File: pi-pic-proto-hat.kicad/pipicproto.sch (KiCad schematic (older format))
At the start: 39 parts, among them J1 RUN/~PGM~, J10 Conn_01x13_Male, J11 Conn_5P_2, J12 Conn_01x01_Male, J13 Conn_01x05_Male, J14 Conn_01x02_Male, J2 Conn_SW1, J22 Conn_01x13_Male, J3 Conn_5P, J4 Conn_3V3P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

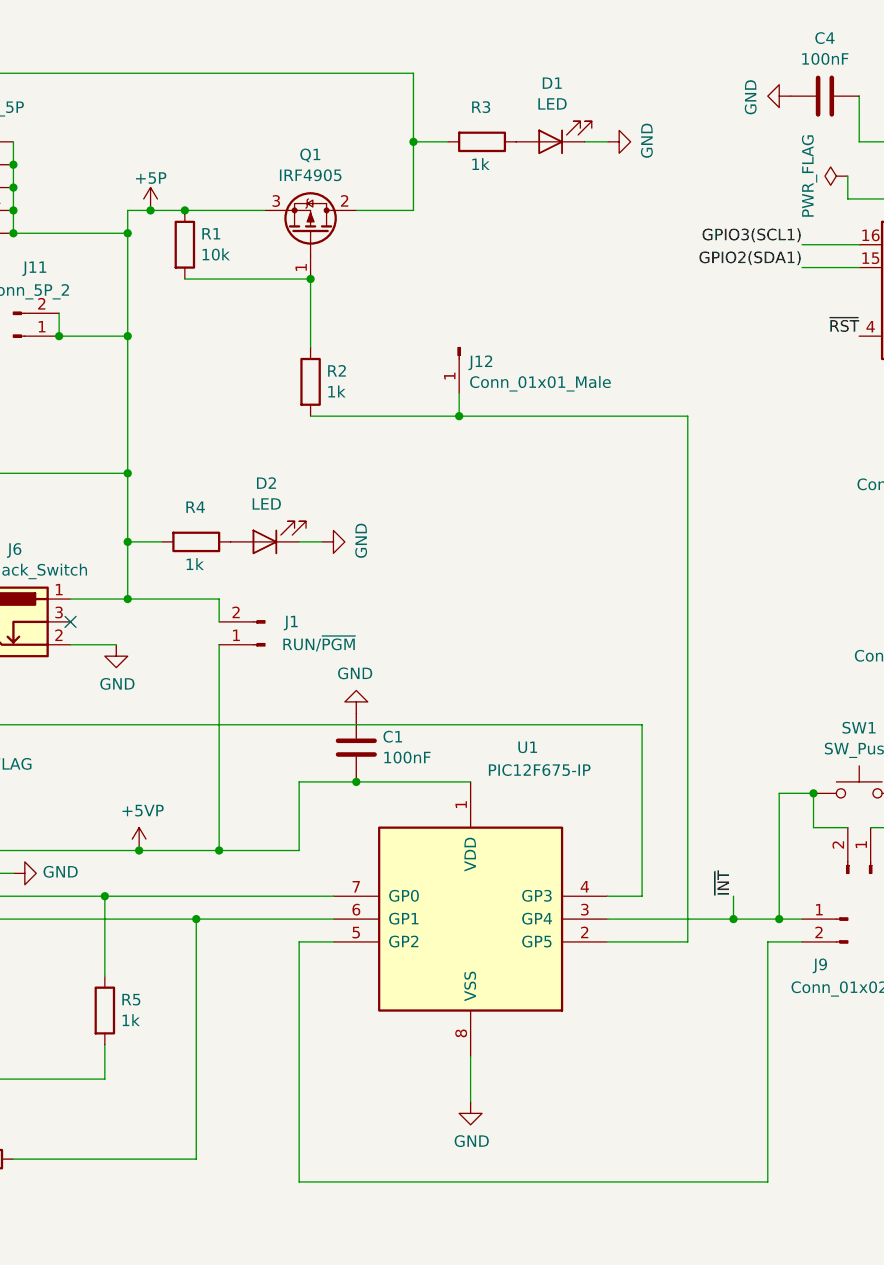
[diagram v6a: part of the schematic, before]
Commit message: non-functional changes to layout
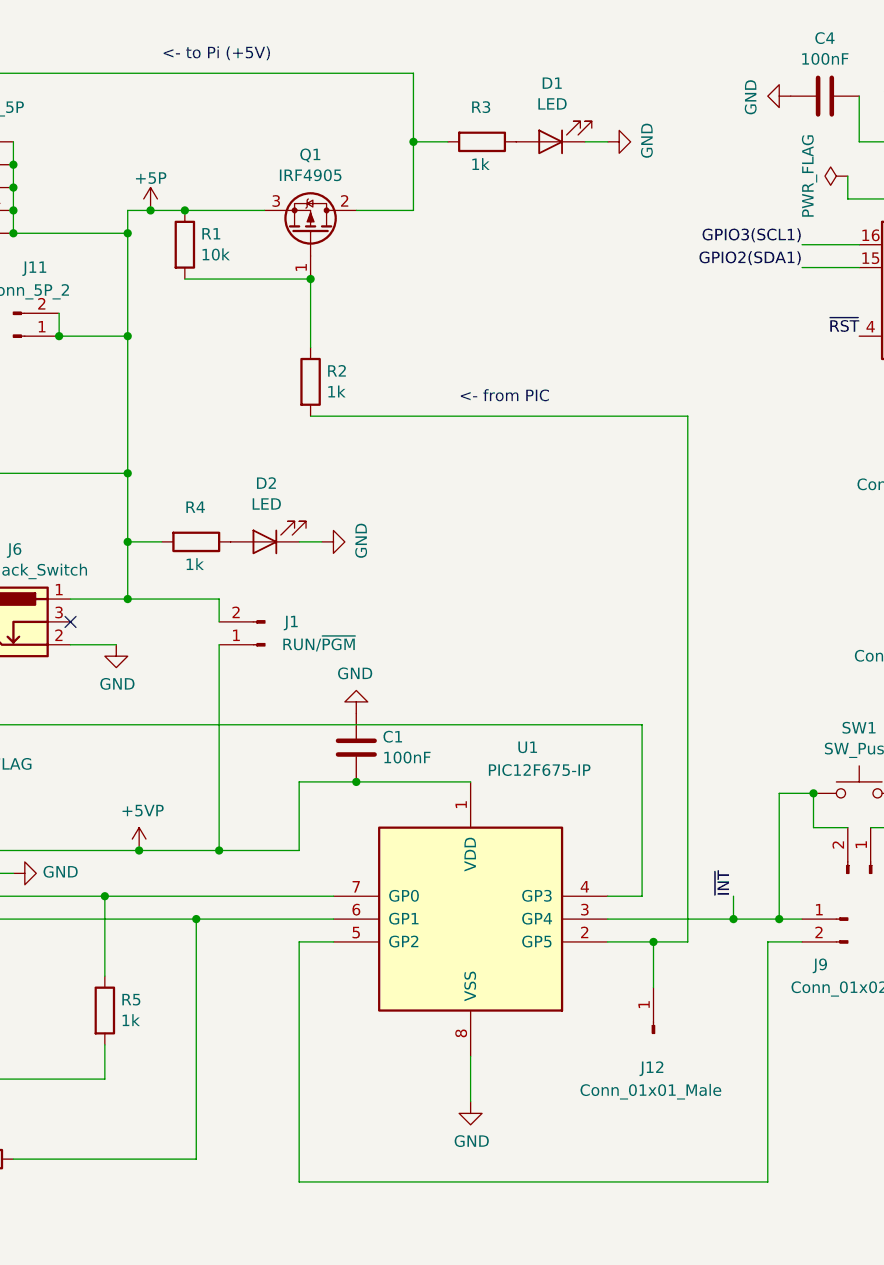
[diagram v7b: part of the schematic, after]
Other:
- note added: "<- from PIC"
- note added: "<- to Pi (+5V)"
- moved on the sheet: J12
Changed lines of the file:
@@
 	1700 4950 1700 5850
 Wire Wire Line
-	8600 4700 8950 4700
-Wire Wire Line
-	8950 4700 8950 2400
-Wire Wire Line
-	8950 2400 7950 2400
+	8600 4700 8800 4700
 Text Label 5850 5300 2    50   ~ 0
 GPIO16
@@
 L Connector:Conn_01x01_Male J12
 U 1 1 5F23F4B8
-P 7950 2100
-F 0 "J12" V 8012 2144 50  0000 L CNN
-F 1 "Conn_01x01_Male" V 8103 2144 50  0000 L CNN
-F 2 "Connector_PinHeader_2.54mm:PinHeader_1x01_P2.54mm_Vertical" H 7950 2100 50  0001 C CNN
-F 3 "~" H 7950 2100 50  0001 C CNN
-	1    7950 2100
-	0    1    1    0
-$EndComp
-Wire Wire Line
-	7950 2400 7950 2300
-Connection ~ 7950 2400
-Wire Wire Line
-	7950 2400 7300 2400
+P 8800 5100
+F 0 "J12" V 8650 5050 50  0000 L CNN
+F 1 "Conn_01x01_Male" V 8550 4800 50  0000 L CNN
+F 2 "Connector_PinHeader_2.54mm:PinHeader_1x01_P2.54mm_Vertical" H 8800 5100 50  0001 C CNN
+F 3 "~" H 8800 5100 50  0001 C CNN
+	1    8800 5100
+	0    -1   -1   0
+$EndComp
 $Comp
 L Timer_RTC:DS3231M U3
@@
 Text Label 9700 2050 2    50   ~ 0
 ~RST
+Wire Wire Line
+	7300 2400 8950 2400
+Wire Wire Line
+	8950 2400 8950 4700
+Wire Wire Line
+	8800 4900 8800 4700
+Connection ~ 8800 4700
+Wire Wire Line
+	8800 4700 8950 4700
+Text Notes 7950 2350 0    50   ~ 0
+<- from PIC
+Text Notes 6650 850  0    50   ~ 0
+<- to Pi (+5V)
 $EndSCHEMATC
